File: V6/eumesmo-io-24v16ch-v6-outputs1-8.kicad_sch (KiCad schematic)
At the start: 5 parts, among them Q4 MMBT2222A

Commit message: Renamed all files to eumesmo branding
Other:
- title: ESP 24V 16xIn/16xOut/1-Wire Module -> eumesmo 24V 16xIn/16xOut/1-Wire Module
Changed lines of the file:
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@@
 	(paper "A4")
 	(title_block
-		(title "ESP 24V 16xIn/16xOut/1-Wire Module")
-		(date "2026-02-10")
-		(rev "V6.1")
+		(title "eumesmo 24V 16xIn/16xOut/1-Wire Module")
+		(date "2026-06-13")
+		(rev "V6.2")
 	)
 	(text "I_{LED} = (24V - V_{LED} - V_{CE}) / 10k\nI_{LED} = (24V - 2.7V - 0,1V) / 10k\nI_{LED} = 2,12 mA"
@@
 		)
 		(instances
-			(project "esp-24v-16ch-v6"
+			(project "eumesmo-io-24v16ch-v6"
 				(path "/2bc5a21a-1d79-419d-a592-6852cc07b00a/032d24f7-dea6-43c8-b36e-6c84d69a3256"
 					(reference "#PWR0231")
@@
 		)
 		(instances
-			(project "esp-24v-16ch-v6"
+			(project "eumesmo-io-24v16ch-v6"
 				(path "/2bc5a21a-1d79-419d-a592-6852cc07b00a/032d24f7-dea6-43c8-b36e-6c84d69a3256"
 					(reference "#PWR0230")
@@
 		)
 		(instances
-			(project "esp-24v-16ch-v6"
+			(project "eumesmo-io-24v16ch-v6"
 				(path "/2bc5a21a-1d79-419d-a592-6852cc07b00a/032d24f7-dea6-43c8-b36e-6c84d69a3256"
 					(reference "R104")
@@
 		)
 		(instances
-			(project "esp-24v-16ch-v6"
+			(project "eumesmo-io-24v16ch-v6"
 				(path "/2bc5a21a-1d79-419d-a592-6852cc07b00a/032d24f7-dea6-43c8-b36e-6c84d69a3256"
 					(reference "R105")
@@
 		)
 		(instances
-			(project "esp-24v-16ch-v6"
+			(project "eumesmo-io-24v16ch-v6"
 				(path "/2bc5a21a-1d79-419d-a592-6852cc07b00a/032d24f7-dea6-43c8-b36e-6c84d69a3256"
 					(reference "D63")
@@
 		)
 		(instances
-			(project "esp-24v-16ch-v6"
+			(project "eumesmo-io-24v16ch-v6"
 				(path "/2bc5a21a-1d79-419d-a592-6852cc07b00a/032d24f7-dea6-43c8-b36e-6c84d69a3256"
 					(reference "R106")
@@
 		)
 		(instances
-			(project "esp-24v-16ch-v6"
+			(project "eumesmo-io-24v16ch-v6"
 				(path "/2bc5a21a-1d79-419d-a592-6852cc07b00a/032d24f7-dea6-43c8-b36e-6c84d69a3256"
 					(reference "#PWR0232")
@@
 		)
 		(instances
-			(project "esp-24v-16ch-v6"
+			(project "eumesmo-io-24v16ch-v6"
 				(path "/2bc5a21a-1d79-419d-a592-6852cc07b00a/032d24f7-dea6-43c8-b36e-6c84d69a3256"
 					(reference "Q9")

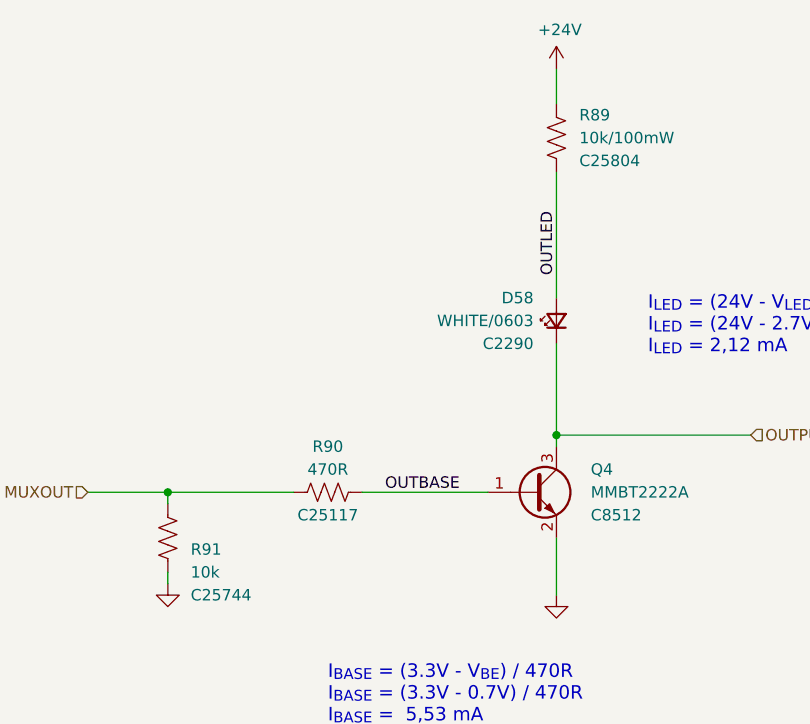
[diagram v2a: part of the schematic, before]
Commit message: Added CPU health LED
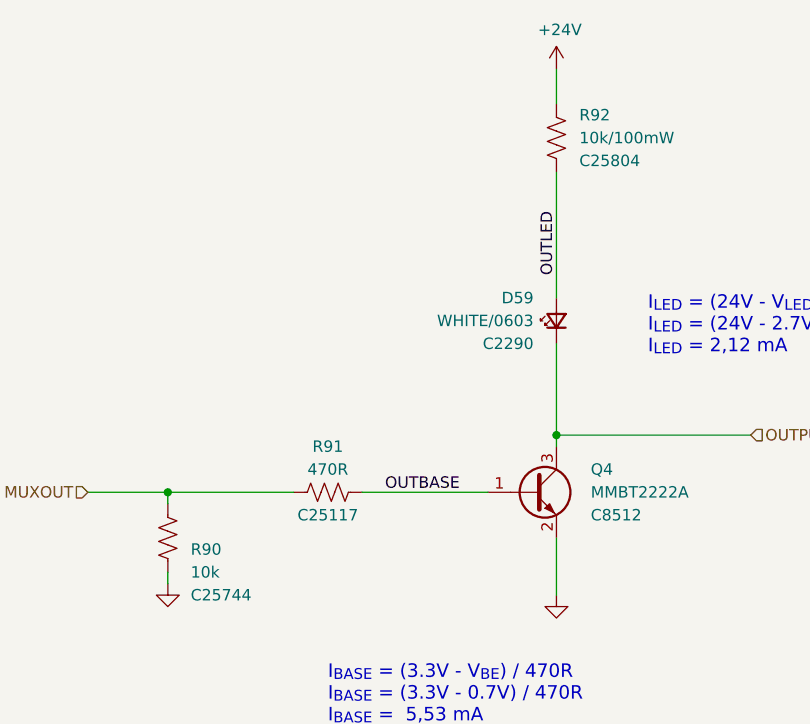
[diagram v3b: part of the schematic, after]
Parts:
- renumbered D58 to D59, R91 to R90, R90 to R91, R89 to R92
